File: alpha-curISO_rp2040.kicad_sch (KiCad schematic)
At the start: 23 parts, among them J2 SWD, U1 RP2040, U5 74AHCT1G125

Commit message: speaker added, sharing pin with bottom left rotary
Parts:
- added LS1: Speaker, Keebio-Parts:AST1109MLTRQ, symbol Device:Speaker
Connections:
- net GND: now also LS1.2
- net R5_A: now also LS1.1
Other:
- note removed: "4 pins free! we can reconnect the rotaries"
- moved on the sheet: C19, U5

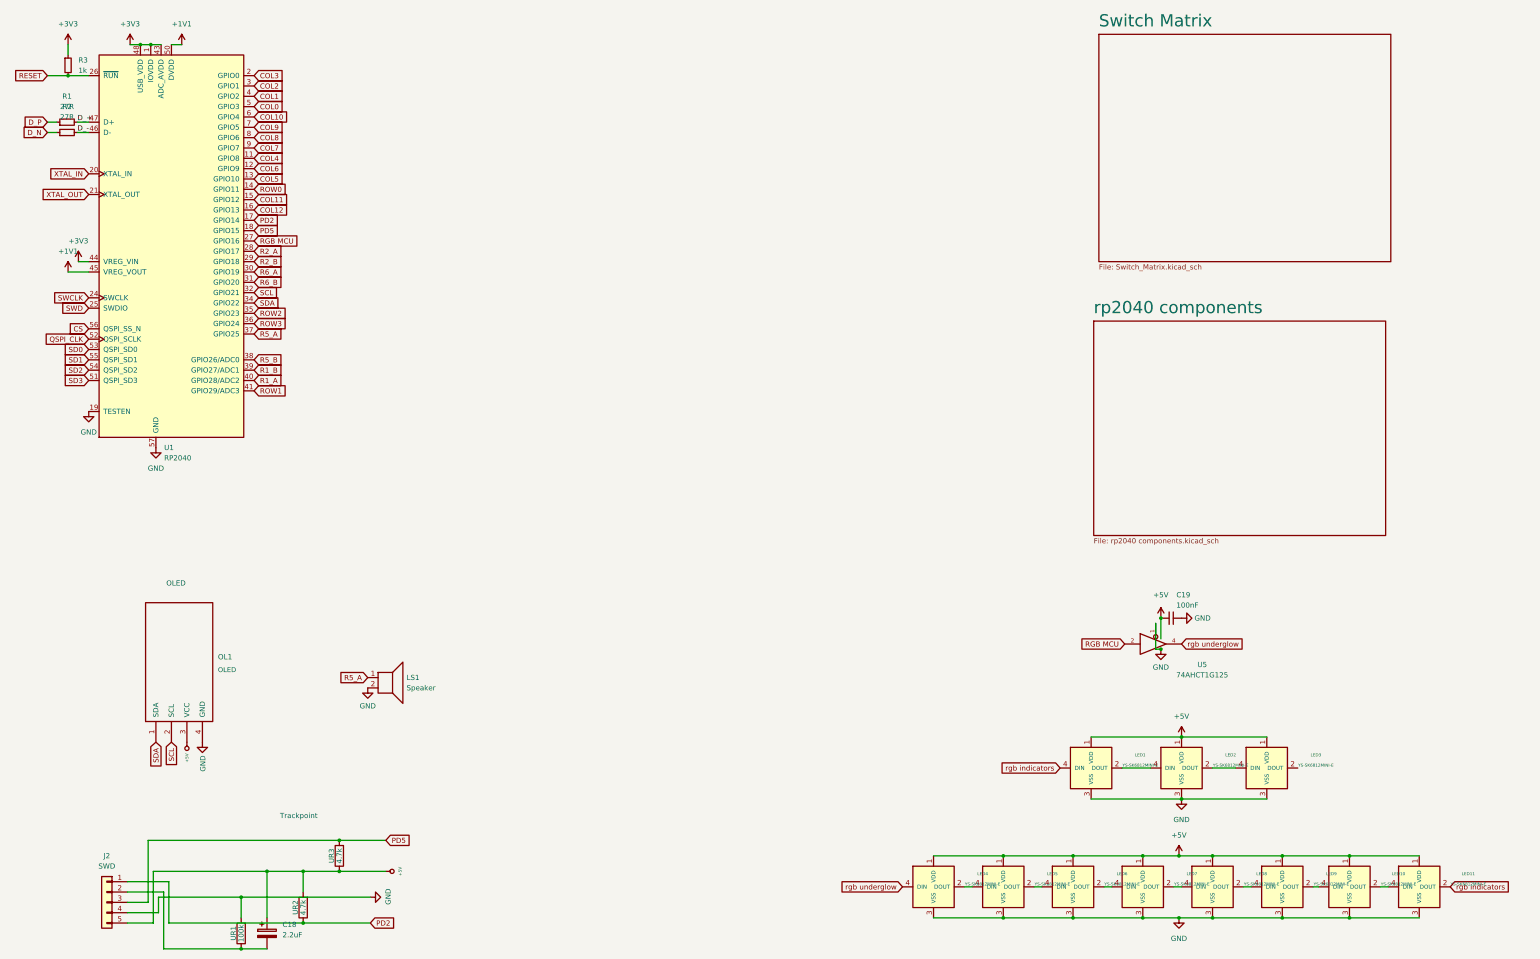
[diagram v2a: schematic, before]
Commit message: finished new PCB draft
ran preliminary DRC
cleaned up project folder
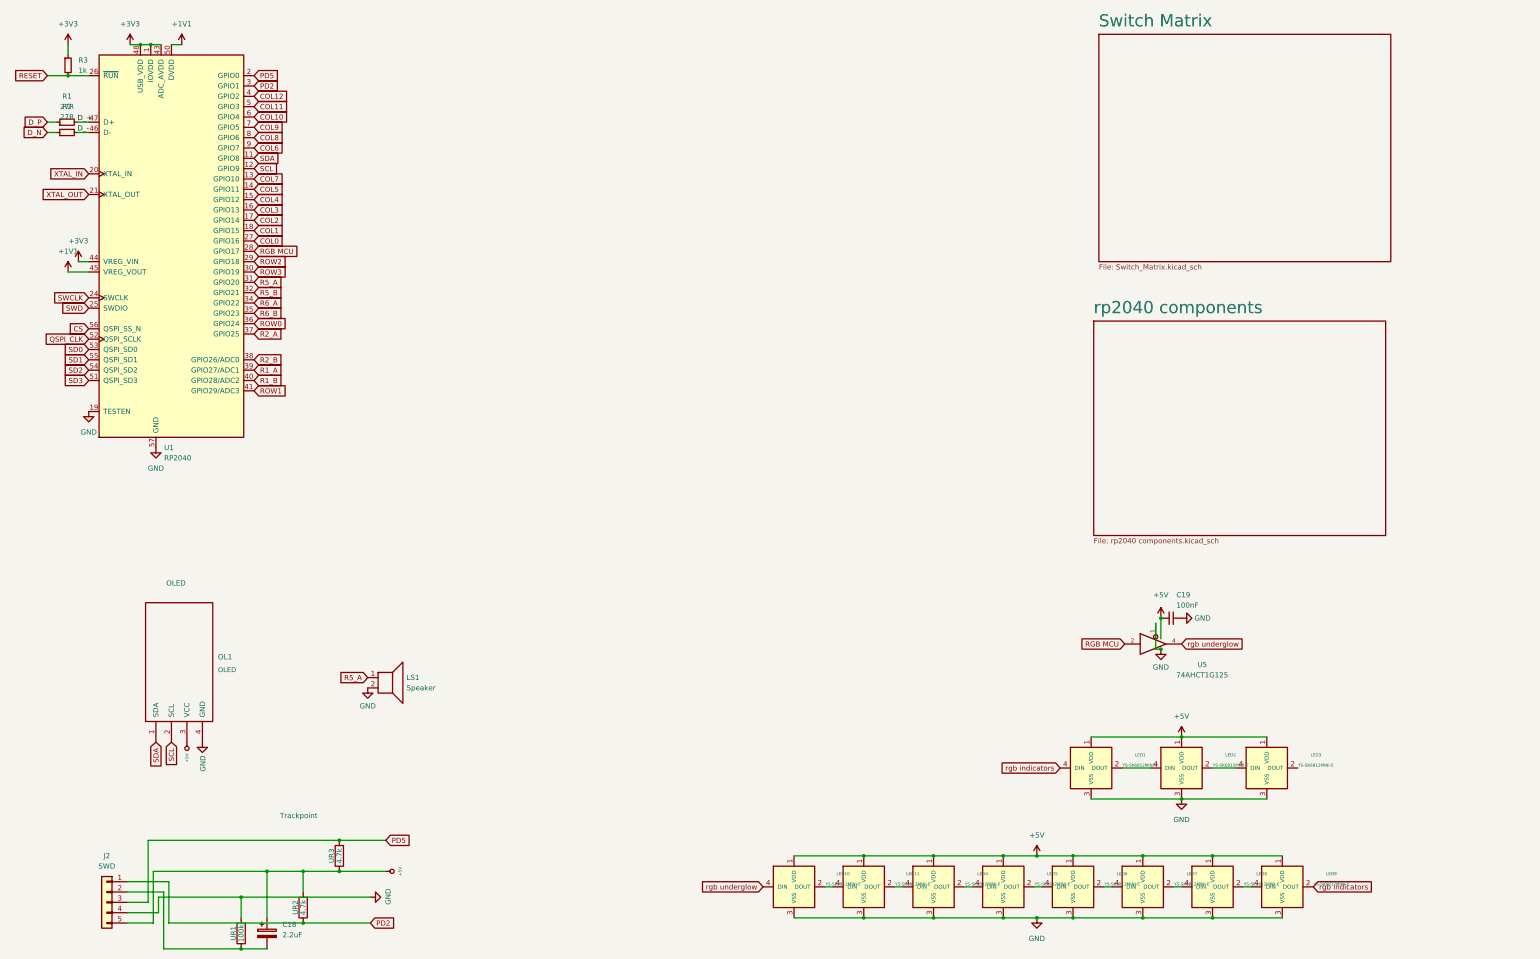
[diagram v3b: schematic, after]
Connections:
- net COL0: now also U1.27 (GPIO16); no longer U1.5 (GPIO3)
- net COL1: now also U1.18 (GPIO15); no longer U1.4 (GPIO2)
- net COL11: now also U1.5 (GPIO3); no longer U1.15 (GPIO12)
- net COL12: now also U1.4 (GPIO2); no longer U1.16 (GPIO13)
- net COL2: now also U1.17 (GPIO14); no longer U1.3 (GPIO1)
- net COL3: now also U1.16 (GPIO13); no longer U1.2 (GPIO0)
- net COL4: now also U1.15 (GPIO12); no longer U1.11 (GPIO8)
- net COL5: now also U1.14 (GPIO11); no longer U1.13 (GPIO10)
- net COL6: now also U1.9 (GPIO7); no longer U1.12 (GPIO9)
- net COL7: now also U1.13 (GPIO10); no longer U1.9 (GPIO7)
- net PD2: now also U1.3 (GPIO1); no longer U1.17 (GPIO14)
- net PD5: now also U1.2 (GPIO0); no longer U1.18 (GPIO15)
- net R1_A: now also U1.39 (GPIO27/ADC1); no longer U1.40 (GPIO28/ADC2)
- net R1_B: now also U1.40 (GPIO28/ADC2); no longer U1.39 (GPIO27/ADC1)
- net R2_A: now also U1.37 (GPIO25); no longer U1.28 (GPIO17)
- net R2_B: now also U1.38 (GPIO26/ADC0); no longer U1.29 (GPIO18)
- net R5_A: now also U1.31 (GPIO20); no longer U1.37 (GPIO25)
- net R5_B: now also U1.32 (GPIO21); no longer U1.38 (GPIO26/ADC0)
- net R6_A: now also U1.34 (GPIO22); no longer U1.30 (GPIO19)
- net R6_B: now also U1.35 (GPIO23); no longer U1.31 (GPIO20)
- net RGB MCU: now also U1.28 (GPIO17); no longer U1.27 (GPIO16)
- net ROW0: now also U1.36 (GPIO24); no longer U1.14 (GPIO11)
- net ROW2: now also U1.29 (GPIO18); no longer U1.35 (GPIO23)
- net ROW3: now also U1.30 (GPIO19); no longer U1.36 (GPIO24)
- net SCL: now also U1.12 (GPIO9); no longer U1.32 (GPIO21)
- net SDA: now also U1.11 (GPIO8); no longer U1.34 (GPIO22)
- net rgb indicators: now also LED9.2 (DOUT); no longer LED11.2 (DOUT)
- net rgb underglow: now also LED10.4 (DIN); no longer LED4.4 (DIN)
- new net: LED11.2 (DOUT), LED4.4 (DIN)
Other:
- moved on the sheet: LED10, LED11
